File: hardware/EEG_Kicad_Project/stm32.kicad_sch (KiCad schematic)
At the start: 14 parts, among them SW1 SW_Push, U1 STM32F446RETx

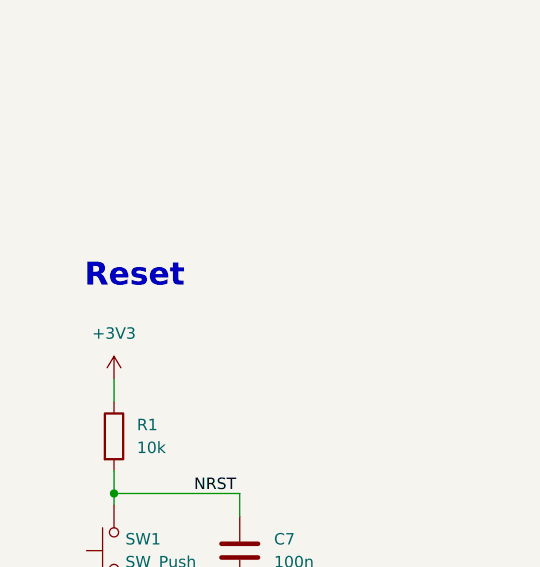
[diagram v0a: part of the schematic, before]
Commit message: Added ADS1299, hierarchical sheets for: power, usb, analog, stm
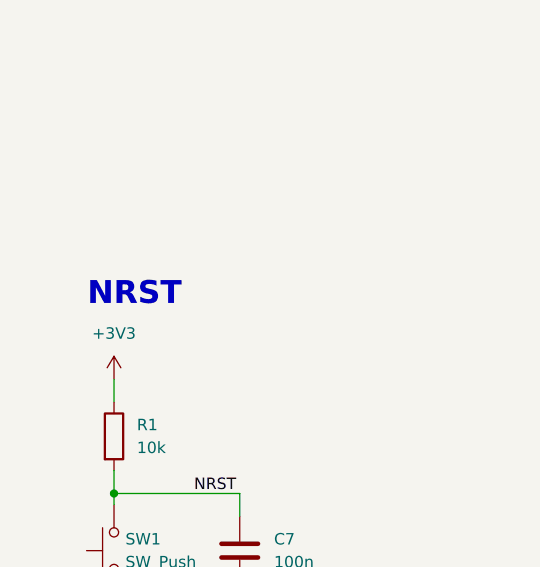
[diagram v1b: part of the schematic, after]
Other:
- note added: "NRST"
- note removed: "Reset"
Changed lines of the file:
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@@
 		)
 	)
-	(text "Reset\n\n"
+	(text "NRST"
 		(exclude_from_sim no)
 		(at 28.956 97.282 0)
@@
 		)
 		(instances
-			(project "EEG Kicad Project"
+			(project "EEG_Kicad_Project"
 				(path "/f077bb96-fdd8-4d67-8482-ecc439e899e7/088aea0a-da05-47a8-ac1b-bdebb168844a"
 					(reference "SW1")
@@
 		)
 		(instances
-			(project "EEG Kicad Project"
+			(project "EEG_Kicad_Project"
 				(path "/f077bb96-fdd8-4d67-8482-ecc439e899e7/088aea0a-da05-47a8-ac1b-bdebb168844a"
 					(reference "#PWR08")
@@
 		)
 		(instances
-			(project "EEG Kicad Project"
+			(project "EEG_Kicad_Project"
 				(path "/f077bb96-fdd8-4d67-8482-ecc439e899e7/088aea0a-da05-47a8-ac1b-bdebb168844a"
 					(reference "#PWR012")
@@
 		)
 		(instances
-			(project "EEG Kicad Project"
+			(project "EEG_Kicad_Project"
 				(path "/f077bb96-fdd8-4d67-8482-ecc439e899e7/088aea0a-da05-47a8-ac1b-bdebb168844a"
 					(reference "#PWR06")
@@
 		)
 		(instances
-			(project "EEG Kicad Project"
+			(project "EEG_Kicad_Project"
 				(path "/f077bb96-fdd8-4d67-8482-ecc439e899e7/088aea0a-da05-47a8-ac1b-bdebb168844a"
 					(reference "#PWR013")
@@
 		)
 		(instances
-			(project "EEG Kicad Project"
+			(project "EEG_Kicad_Project"
 				(path "/f077bb96-fdd8-4d67-8482-ecc439e899e7/088aea0a-da05-47a8-ac1b-bdebb168844a"
 					(reference "R2")
@@
 		)
 		(instances
-			(project "EEG Kicad Project"
+			(project "EEG_Kicad_Project"
 				(path "/f077bb96-fdd8-4d67-8482-ecc439e899e7/088aea0a-da05-47a8-ac1b-bdebb168844a"
 					(reference "C4")
@@
 		)
 		(instances
-			(project "EEG Kicad Project"
+			(project "EEG_Kicad_Project"
 				(path "/f077bb96-fdd8-4d67-8482-ecc439e899e7/088aea0a-da05-47a8-ac1b-bdebb168844a"
 					(reference "C1")
@@
 		)
 		(instances
-			(project "EEG Kicad Project"
+			(project "EEG_Kicad_Project"
 				(path "/f077bb96-fdd8-4d67-8482-ecc439e899e7/088aea0a-da05-47a8-ac1b-bdebb168844a"
 					(reference "C8")
@@
 		)
 		(instances
-			(project "EEG Kicad Project"
+			(project "EEG_Kicad_Project"
 				(path "/f077bb96-fdd8-4d67-8482-ecc439e899e7/088aea0a-da05-47a8-ac1b-bdebb168844a"
 					(reference "C7")
@@
 		)
 		(instances
-			(project "EEG Kicad Project"
+			(project "EEG_Kicad_Project"
 				(path "/f077bb96-fdd8-4d67-8482-ecc439e899e7/088aea0a-da05-47a8-ac1b-bdebb168844a"
 					(reference "C2")
@@
 		)
 		(instances
-			(project "EEG Kicad Project"
+			(project "EEG_Kicad_Project"
 				(path "/f077bb96-fdd8-4d67-8482-ecc439e899e7/088aea0a-da05-47a8-ac1b-bdebb168844a"
 					(reference "#PWR011")
@@
 		)
 		(instances
-			(project "EEG Kicad Project"
+			(project "EEG_Kicad_Project"
 				(path "/f077bb96-fdd8-4d67-8482-ecc439e899e7/088aea0a-da05-47a8-ac1b-bdebb168844a"
 					(reference "#PWR07")
@@
 		)
 		(instances
-			(project "EEG Kicad Project"
+			(project "EEG_Kicad_Project"
 				(path "/f077bb96-fdd8-4d67-8482-ecc439e899e7/088aea0a-da05-47a8-ac1b-bdebb168844a"
 					(reference "JP1")
@@
 		)
 		(instances
-			(project "EEG Kicad Project"
+			(project "EEG_Kicad_Project"
 				(path "/f077bb96-fdd8-4d67-8482-ecc439e899e7/088aea0a-da05-47a8-ac1b-bdebb168844a"
 					(reference "R1")
@@
 		)
 		(instances
-			(project "EEG Kicad Project"
+			(project "EEG_Kicad_Project"
 				(path "/f077bb96-fdd8-4d67-8482-ecc439e899e7/088aea0a-da05-47a8-ac1b-bdebb168844a"
 					(reference "C5")
@@
 		)
 		(instances
-			(project "EEG Kicad Project"
+			(project "EEG_Kicad_Project"
 				(path "/f077bb96-fdd8-4d67-8482-ecc439e899e7/088aea0a-da05-47a8-ac1b-bdebb168844a"
 					(reference "C9")
@@
 		)
 		(instances
-			(project "EEG Kicad Project"
+			(project "EEG_Kicad_Project"
 				(path "/f077bb96-fdd8-4d67-8482-ecc439e899e7/088aea0a-da05-47a8-ac1b-bdebb168844a"
 					(reference "#PWR010")
@@
 		)
 		(instances
-			(project "EEG Kicad Project"
+			(project "EEG_Kicad_Project"
 				(path "/f077bb96-fdd8-4d67-8482-ecc439e899e7/088aea0a-da05-47a8-ac1b-bdebb168844a"
 					(reference "C3")
@@
 		)
 		(instances
-			(project "EEG Kicad Project"
+			(project "EEG_Kicad_Project"
 				(path "/f077bb96-fdd8-4d67-8482-ecc439e899e7/088aea0a-da05-47a8-ac1b-bdebb168844a"
 					(reference "C6")
@@
 		)
 		(instances
-			(project "EEG Kicad Project"
+			(project "EEG_Kicad_Project"
 				(path "/f077bb96-fdd8-4d67-8482-ecc439e899e7/088aea0a-da05-47a8-ac1b-bdebb168844a"
 					(reference "#PWR09")
@@
 		)
 		(instances
-			(project "EEG Kicad Project"
+			(project "EEG_Kicad_Project"
 				(path "/f077bb96-fdd8-4d67-8482-ecc439e899e7/088aea0a-da05-47a8-ac1b-bdebb168844a"
 					(reference "#PWR03")
@@
 		)
 		(instances
-			(project "EEG Kicad Project"
+			(project "EEG_Kicad_Project"
 				(path "/f077bb96-fdd8-4d67-8482-ecc439e899e7/088aea0a-da05-47a8-ac1b-bdebb168844a"
 					(reference "U1")
